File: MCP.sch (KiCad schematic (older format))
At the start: 2 parts

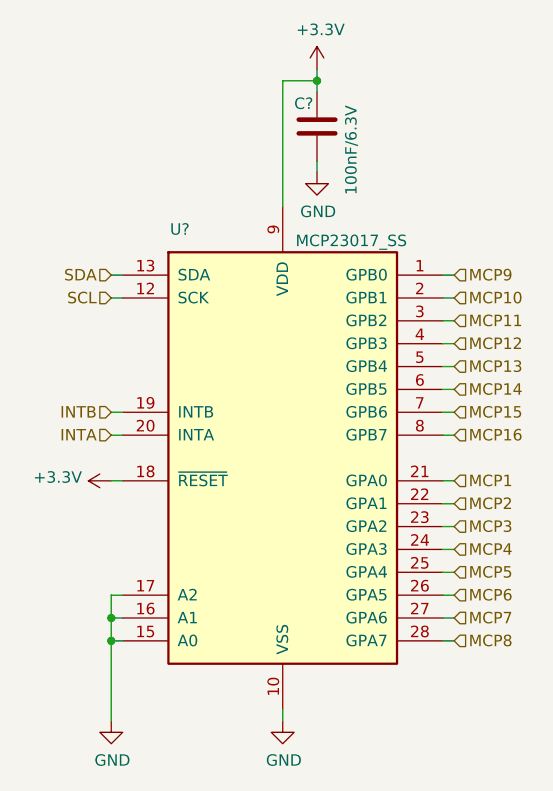
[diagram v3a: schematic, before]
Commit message: Exported first net
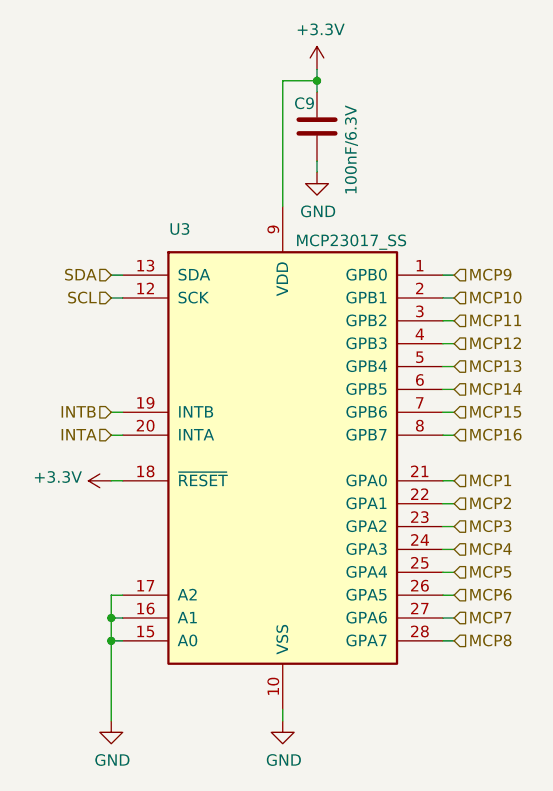
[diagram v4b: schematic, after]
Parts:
- gave numbers to parts that had none: 2
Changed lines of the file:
@@
 $EndDescr
 $Comp
-L Interface_Expansion:MCP23017_SS U?
+L Interface_Expansion:MCP23017_SS U3
 U 1 1 6215ABA4
 P 5850 3900
-F 0 "U?" H 5400 4900 50  0000 C CNN
+F 0 "U3" H 5400 4900 50  0000 C CNN
 F 1 "MCP23017_SS" H 6150 4850 50  0000 C CNN
 F 2 "Package_SO:SSOP-28_5.3x10.2mm_P0.65mm" H 6050 2900 50  0001 L CNN
@@
 P 6000 2450
 AR Path="/6212150F/6215C507" Ref="C?"  Part="1"
-AR Path="/6215A73B/6215C507" Ref="C?"  Part="1"
-F 0 "C?" H 5900 2550 50  0000 L CNN
+AR Path="/6215A73B/6215C507" Ref="C9"  Part="1"
+F 0 "C9" H 5900 2550 50  0000 L CNN
 F 1 "100nF/6.3V" V 6150 2150 50  0000 L CNN
 F 2 "Capacitor_SMD:C_0402_1005Metric" H 6038 2300 50  0001 C CNN
@@
 $EndComp
 $Comp
-L power:GND #PWR?
+L power:GND #PWR0120
 U 1 1 6215C81C
 P 6000 2650
-F 0 "#PWR?" H 6000 2400 50  0001 C CNN
+F 0 "#PWR0120" H 6000 2400 50  0001 C CNN
 F 1 "GND" H 6005 2477 50  0000 C CNN
 F 2 "" H 6000 2650 50  0001 C CNN
@@
 Connection ~ 6000 2250
 $Comp
-L power:+3.3V #PWR?
+L power:+3.3V #PWR0121
 U 1 1 6215D18D
 P 6000 2200
-F 0 "#PWR?" H 6000 2050 50  0001 C CNN
+F 0 "#PWR0121" H 6000 2050 50  0001 C CNN
 F 1 "+3.3V" H 6015 2373 50  0000 C CNN
 F 2 "" H 6000 2200 50  0001 C CNN
@@
 INTA
 $Comp
-L power:+3.3V #PWR?
+L power:+3.3V #PWR0122
 U 1 1 6215DC1B
 P 5100 4000
-F 0 "#PWR?" H 5100 3850 50  0001 C CNN
+F 0 "#PWR0122" H 5100 3850 50  0001 C CNN
 F 1 "+3.3V" V 5115 4128 50  0000 L CNN
 F 2 "" H 5100 4000 50  0001 C CNN
@@
 $EndComp
 $Comp
-L power:GND #PWR?
+L power:GND #PWR0123
 U 1 1 6215E536
 P 5850 5050
-F 0 "#PWR?" H 5850 4800 50  0001 C CNN
+F 0 "#PWR0123" H 5850 4800 50  0001 C CNN
 F 1 "GND" H 5855 4877 50  0000 C CNN
 F 2 "" H 5850 5050 50  0001 C CNN
@@
 $EndComp
 $Comp
-L power:GND #PWR?
+L power:GND #PWR0124
 U 1 1 6215ECB2
 P 5100 5050
-F 0 "#PWR?" H 5100 4800 50  0001 C CNN
+F 0 "#PWR0124" H 5100 4800 50  0001 C CNN
 F 1 "GND" H 5105 4877 50  0000 C CNN
 F 2 "" H 5100 5050 50  0001 C CNN

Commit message: Added lcsc part nums
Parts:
- C9: value 100nF/6.3V -> 100nF/50V/10%; LCSC (none) -> C307331
- U3: LCSC (none) -> C153287
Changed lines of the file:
@@
 F 2 "Package_SO:SSOP-28_5.3x10.2mm_P0.65mm" H 6050 2900 50  0001 L CNN
 F 3 "http://ww1.microchip.com/downloads/en/DeviceDoc/20001952C.pdf" H 6050 2800 50  0001 L CNN
+F 4 "C153287" H 5850 3900 50  0001 C CNN "LCSC"
 	1    5850 3900
 	1    0    0    -1
@@
 AR Path="/6215A73B/6215C507" Ref="C9"  Part="1"
 F 0 "C9" H 5900 2550 50  0000 L CNN
-F 1 "100nF/6.3V" V 6150 2150 50  0000 L CNN
+F 1 "100nF/50V/10%" V 6150 2150 50  0000 L CNN
 F 2 "Capacitor_SMD:C_0402_1005Metric" H 6038 2300 50  0001 C CNN
 F 3 "~" H 6000 2450 50  0001 C CNN
+F 4 "C307331" H 6000 2450 50  0001 C CNN "LCSC"
 	1    6000 2450
 	1    0    0    -1
